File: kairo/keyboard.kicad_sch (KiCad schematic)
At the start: 1 part, among them U1 ProMicro

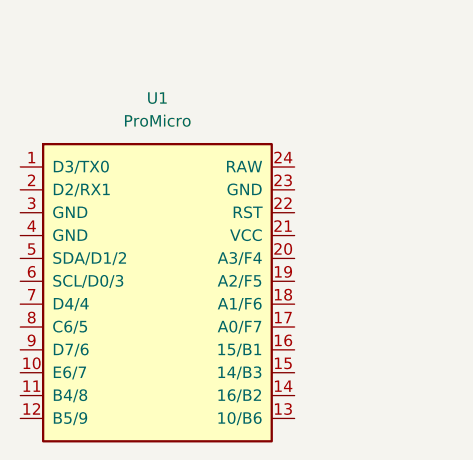
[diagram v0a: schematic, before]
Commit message: テストでキースイッチの追加
テスト用
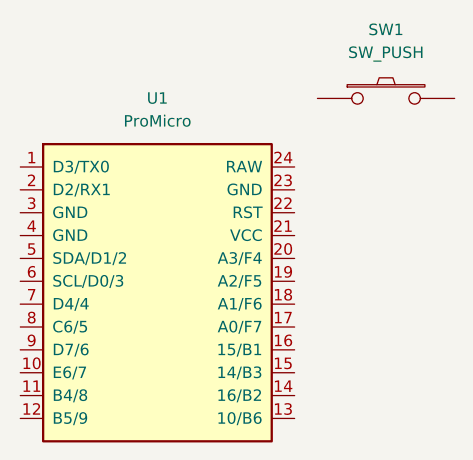
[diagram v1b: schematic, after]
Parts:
- added SW1: SW_PUSH, BrownSugar_KBD:Kailh_Choc_V1_Hotswap_via, symbol BrownSugar_KBD:SW_PUSH
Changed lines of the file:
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@@
 	(paper "A4")
+	(symbol
+		(lib_id "BrownSugar_KBD:SW_PUSH")
+		(at 72.39 44.45 0)
+		(unit 1)
+		(exclude_from_sim no)
+		(in_bom yes)
+		(on_board yes)
+		(dnp no)
+		(fields_autoplaced yes)
+		(property "Reference" "SW1"
+			(at 72.39 36.83 0)
+			(effects
+				(font
+					(size 1.27 1.27)
+				)
+			)
+		)
+		(property "Value" "SW_PUSH"
+			(at 72.39 39.37 0)
+			(effects
+				(font
+					(size 1.27 1.27)
+				)
+			)
+		)
+		(property "Footprint" "BrownSugar_KBD:Kailh_Choc_V1_Hotswap_via"
+			(at 72.39 44.45 0)
+			(effects
+				(font
+					(size 1.27 1.27)
+				)
+				(hide yes)
+			)
+		)
+		(property "Datasheet" ""
+			(at 72.39 44.45 0)
+			(effects
+				(font
+					(size 1.27 1.27)
+				)
+			)
+		)
+		(property "Description" ""
+			(at 72.39 44.45 0)
+			(effects
+				(font
+					(size 1.27 1.27)
+				)
+				(hide yes)
+			)
+		)
+		(pin "2"
+		)
+		(pin "1"
+		)
+		(instances
+			(project ""
+				(path "/d147172f-388d-45d2-a744-6b445613309a"
+					(reference "SW1")
+					(unit 1)
+				)
+			)
+		)
+	)
 	(symbol
 		(lib_id "BrownSugar_KBD:ProMicro")
